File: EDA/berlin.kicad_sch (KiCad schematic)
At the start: 615 parts, among them J1 TYPE-C-31-M12_13, SW1,1 Rotary_Encoder_Switch_Chassis, SW1,10 MXSwitch, SW1,11 MXSwitch, SW1,12 MXSwitch, SW1,13 MXSwitch, SW1,14 MXSwitch, SW1,15 MXSwitch, SW1,16 Rotary_Encoder_Switch_Chassis, SW1,2 MXSwitch, SW1,3 MXSwitch, SW1,4 MXSwitch, SW1,5 MXSwitch, SW1,6 MXSwitch, SW1,7 MXSwitch, SW1,8 MXSwitch, SW1,9 MXSwitch, SW2,1 MXSwitch, SW2,10 MXSwitch, SW2,11 MXSwitch, SW2,12 MXSwitch, SW2,13 MXSwitch, SW2,14 MXSwitch, SW2,15 MXSwitch, SW2,16 MXSwitch, SW2,17 MXSwitch, SW2,18 MXSwitch, SW2,19 MXSwitch, SW2,2 MXSwitch, SW2,3 MXSwitch, SW2,4 MXSwitch, SW2,5 MXSwitch, SW2,6 MXSwitch, SW2,7 MXSwitch, SW2,9 MXSwitch, SW20-7,3 MXSwitch, SW3,1 MXSwitch, SW3,10 MXSwitch, SW3,11 MXSwitch, SW3,12 MXSwitch, SW3,13 MXSwitch, SW3,14 MXSwitch, SW3,15 MXSwitch, SW3,16 MXSwitch, SW3,17 MXSwitch, SW3,18 MXSwitch, SW3,19 MXSwitch, SW3,2 MXSwitch, SW3,3 MXSwitch, SW3,4 MXSwitch, SW3,5 MXSwitch, SW3,6 MXSwitch, SW3,7 MXSwitch, SW3,8 MXSwitch, SW3,9 MXSwitch, SW39-7,6 MXSwitch, SW4,1 MXSwitch, SW4,10 MXSwitch, SW4,11 MXSwitch, SW4,12 MXSwitch, SW4,13 MXSwitch, SW4,14 MXSwitch, SW4,15 MXSwitch, SW4,16 MXSwitch, SW4,17 MXSwitch, SW4,18 MXSwitch, SW4,19 MXSwitch, SW4,2 MXSwitch, SW4,3 MXSwitch, SW4,4 MXSwitch, SW4,5 MXSwitch, SW4,6 MXSwitch, SW4,7 MXSwitch, SW4,8 MXSwitch, SW4,9 MXSwitch, SW5,1 MXSwitch, SW5,10 MXSwitch, SW5,11 MXSwitch, SW5,12 MXSwitch, SW5,13 MXSwitch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

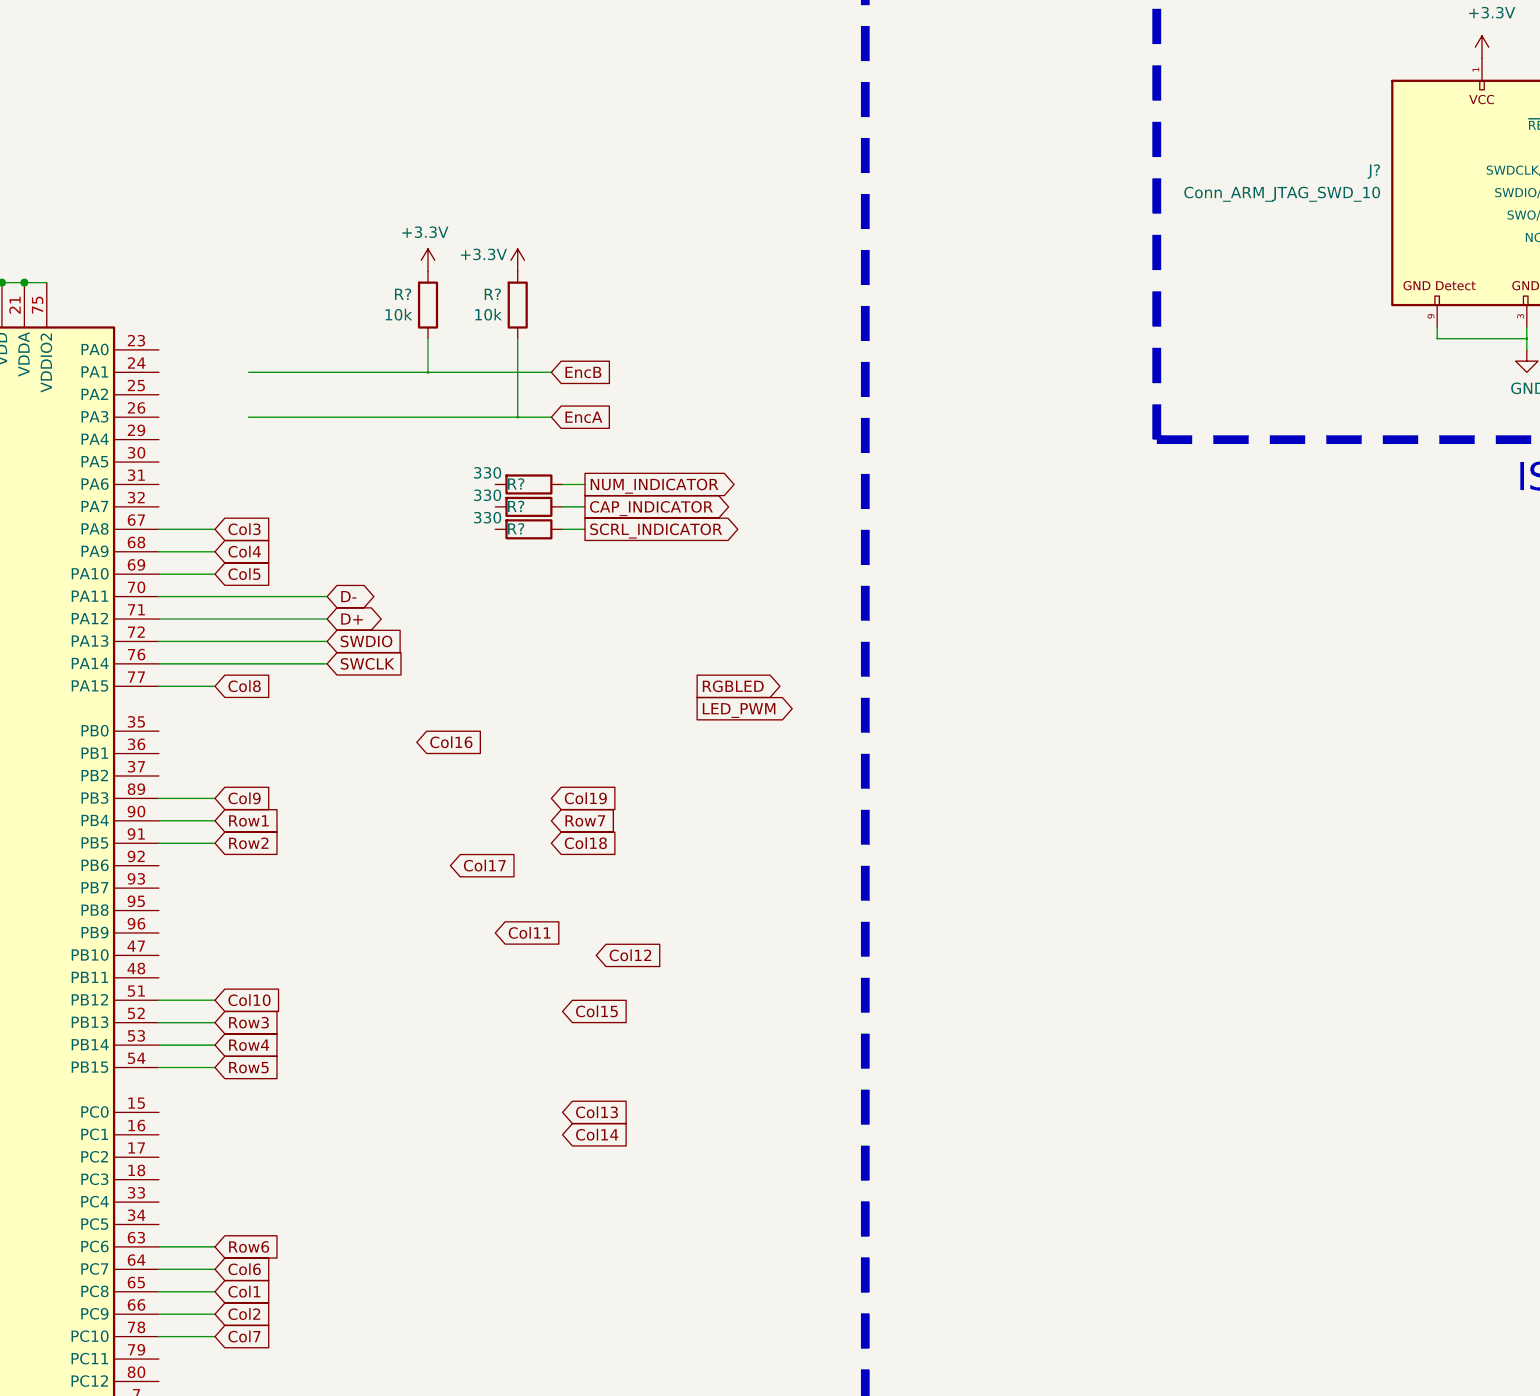
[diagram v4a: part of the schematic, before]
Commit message: route jtag and last key traces
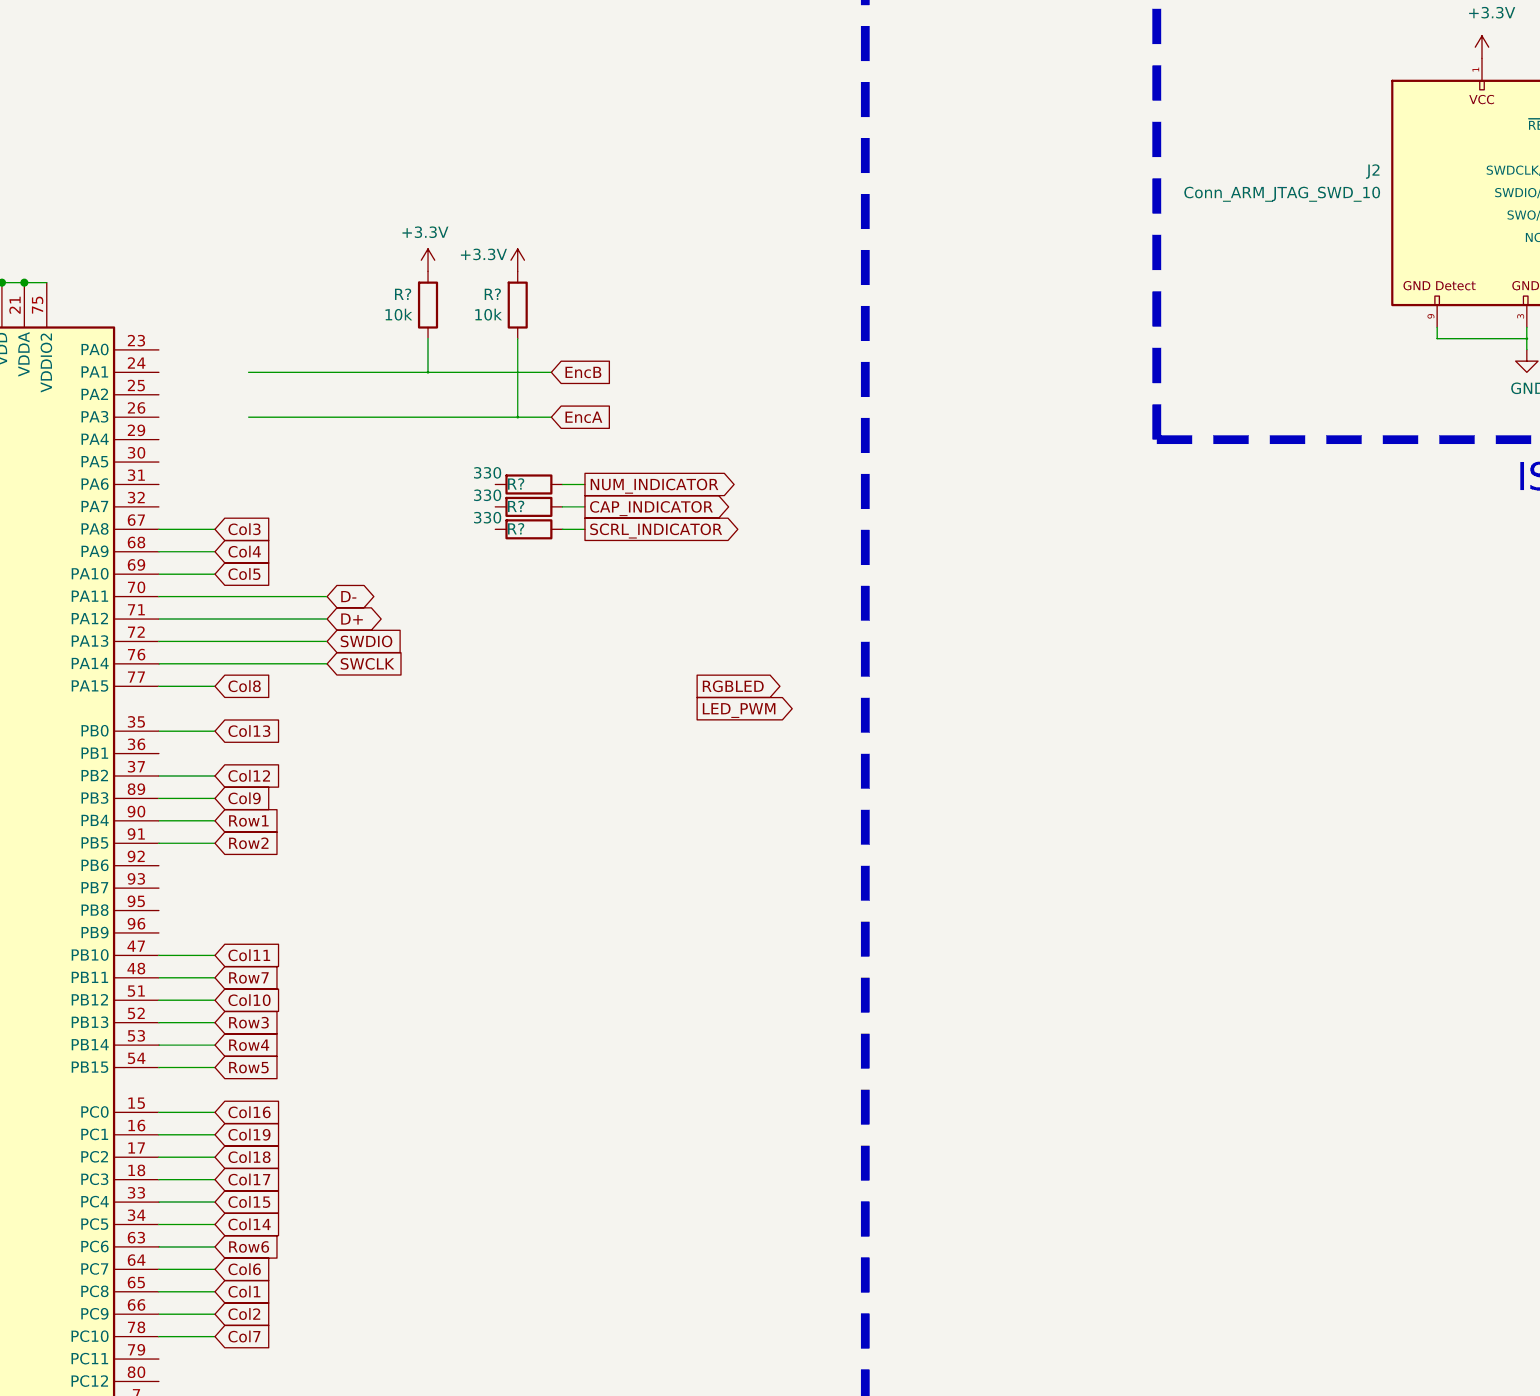
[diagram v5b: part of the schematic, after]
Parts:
- gave numbers to parts that had none: 1
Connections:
- net Col11: now also U1001.47 (PB10)
- net Col12: now also U1001.37 (PB2)
- net Col13: now also U1001.35 (PB0)
- net Col14: now also U1001.34 (PC5)
- net Col15: now also U1001.33 (PC4)
- net Col16: now also U1001.15 (PC0)
- net Col17: now also U1001.18 (PC3)
- net Col18: now also U1001.17 (PC2)
- net Col19: now also U1001.16 (PC1)
- net Row7: now also U1001.48 (PB11)
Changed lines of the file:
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@@
     (stroke (width 0) (type solid) (color 0 0 0 0))
   )
+  (wire (pts (xy 839.47 281.94) (xy 845.82 281.94))
+    (stroke (width 0) (type solid) (color 0 0 0 0))
+  )
+  (wire (pts (xy 839.47 287.02) (xy 845.82 287.02))
+    (stroke (width 0) (type solid) (color 0 0 0 0))
+  )
   (wire (pts (xy 839.47 289.56) (xy 845.82 289.56))
     (stroke (width 0) (type solid) (color 0 0 0 0))
@@
     (stroke (width 0) (type solid) (color 0 0 0 0))
   )
+  (wire (pts (xy 839.47 307.34) (xy 845.82 307.34))
+    (stroke (width 0) (type solid) (color 0 0 0 0))
+  )
+  (wire (pts (xy 839.47 309.88) (xy 845.82 309.88))
+    (stroke (width 0) (type solid) (color 0 0 0 0))
+  )
   (wire (pts (xy 839.47 312.42) (xy 845.82 312.42))
     (stroke (width 0) (type solid) (color 0 0 0 0))
@@
     (stroke (width 0) (type solid) (color 0 0 0 0))
   )
+  (wire (pts (xy 839.47 325.12) (xy 845.82 325.12))
+    (stroke (width 0) (type solid) (color 0 0 0 0))
+  )
+  (wire (pts (xy 839.47 327.66) (xy 845.82 327.66))
+    (stroke (width 0) (type solid) (color 0 0 0 0))
+  )
+  (wire (pts (xy 839.47 330.2) (xy 845.82 330.2))
+    (stroke (width 0) (type solid) (color 0 0 0 0))
+  )
+  (wire (pts (xy 839.47 332.74) (xy 845.82 332.74))
+    (stroke (width 0) (type solid) (color 0 0 0 0))
+  )
+  (wire (pts (xy 839.47 335.28) (xy 845.82 335.28))
+    (stroke (width 0) (type solid) (color 0 0 0 0))
+  )
+  (wire (pts (xy 839.47 337.82) (xy 845.82 337.82))
+    (stroke (width 0) (type solid) (color 0 0 0 0))
+  )
   (wire (pts (xy 839.47 340.36) (xy 845.82 340.36))
     (stroke (width 0) (type solid) (color 0 0 0 0))
@@
     )
   )
+  (global_label "Col13" (shape input) (at 845.82 281.94 0)
+    (effects (font (size 1.27 1.27)) (justify left))
+    (property "Intersheet References" "${INTERSHEET_REFS}" (id 0) (at 1294.13 -46.99 0)
+      (effects (font (size 1.27 1.27)) (justify left) hide)
+    )
+  )
+  (global_label "Col12" (shape input) (at 845.82 287.02 0)
+    (effects (font (size 1.27 1.27)) (justify left))
+    (property "Intersheet References" "${INTERSHEET_REFS}" (id 0) (at 1295.4 -34.29 0)
+      (effects (font (size 1.27 1.27)) (justify left) hide)
+    )
+  )
   (global_label "Col9" (shape input) (at 845.82 289.56 0)
     (effects (font (size 1.27 1.27)) (justify left))
@@
     )
   )
+  (global_label "Col11" (shape input) (at 845.82 307.34 0)
+    (effects (font (size 1.27 1.27)) (justify left))
+    (property "Intersheet References" "${INTERSHEET_REFS}" (id 0) (at 1295.4 -11.43 0)
+      (effects (font (size 1.27 1.27)) (justify left) hide)
+    )
+  )
+  (global_label "Row7" (shape input) (at 845.82 309.88 0)
+    (effects (font (size 1.27 1.27)) (justify left))
+    (property "Intersheet References" "${INTERSHEET_REFS}" (id 0) (at 353.06 -11.43 0)
+      (effects (font (size 1.27 1.27)) hide)
+    )
+  )
   (global_label "Col10" (shape input) (at 845.82 312.42 0)
     (effects (font (size 1.27 1.27)) (justify left))
@@
     )
   )
+  (global_label "Col16" (shape input) (at 845.82 325.12 0)
+    (effects (font (size 1.27 1.27)) (justify left))
+    (property "Intersheet References" "${INTERSHEET_REFS}" (id 0) (at 1294.13 21.59 0)
+      (effects (font (size 1.27 1.27)) (justify left) hide)
+    )
+  )
+  (global_label "Col19" (shape input) (at 845.82 327.66 0)
+    (effects (font (size 1.27 1.27)) (justify left))
+    (property "Intersheet References" "${INTERSHEET_REFS}" (id 0) (at 353.06 8.89 0)
+      (effects (font (size 1.27 1.27)) hide)
+    )
+  )
+  (global_label "Col18" (shape input) (at 845.82 330.2 0)
+    (effects (font (size 1.27 1.27)) (justify left))
+    (property "Intersheet References" "${INTERSHEET_REFS}" (id 0) (at 1294.13 36.83 0)
+      (effects (font (size 1.27 1.27)) (justify left) hide)
+    )
+  )
+  (global_label "Col17" (shape input) (at 845.82 332.74 0)
+    (effects (font (size 1.27 1.27)) (justify left))
+    (property "Intersheet References" "${INTERSHEET_REFS}" (id 0) (at 1294.13 26.67 0)
+      (effects (font (size 1.27 1.27)) (justify left) hide)
+    )
+  )
+  (global_label "Col15" (shape input) (at 845.82 335.28 0)
+    (effects (font (size 1.27 1.27)) (justify left))
+    (property "Intersheet References" "${INTERSHEET_REFS}" (id 0) (at 1295.4 1.27 0)
+      (effects (font (size 1.27 1.27)) (justify left) hide)
+    )
+  )
+  (global_label "Col14" (shape input) (at 845.82 337.82 0)
+    (effects (font (size 1.27 1.27)) (justify left))
+    (property "Intersheet References" "${INTERSHEET_REFS}" (id 0) (at 1295.4 6.35 0)
+      (effects (font (size 1.27 1.27)) (justify left) hide)
+    )
+  )
   (global_label "Row6" (shape input) (at 845.82 340.36 0)
     (effects (font (size 1.27 1.27)) (justify left))
@@
     )
   )
-  (global_label "Col16" (shape input) (at 868.68 283.21 0)
-    (effects (font (size 1.27 1.27)) (justify left))
-    (property "Intersheet References" "${INTERSHEET_REFS}" (id 0) (at 1316.99 -20.32 0)
-      (effects (font (size 1.27 1.27)) (justify left) hide)
-    )
-  )
-  (global_label "Col17" (shape input) (at 872.49 297.18 0)
-    (effects (font (size 1.27 1.27)) (justify left))
-    (property "Intersheet References" "${INTERSHEET_REFS}" (id 0) (at 1320.8 -8.89 0)
-      (effects (font (size 1.27 1.27)) (justify left) hide)
-    )
-  )
-  (global_label "Col11" (shape input) (at 877.57 304.8 0)
-    (effects (font (size 1.27 1.27)) (justify left))
-    (property "Intersheet References" "${INTERSHEET_REFS}" (id 0) (at 1327.15 -13.97 0)
-      (effects (font (size 1.27 1.27)) (justify left) hide)
-    )
-  )
   (global_label "EncB" (shape input) (at 883.92 241.3 0)
     (effects (font (size 1.27 1.27)) (justify left))
@@
     )
   )
-  (global_label "Col19" (shape input) (at 883.92 289.56 0)
-    (effects (font (size 1.27 1.27)) (justify left))
-    (property "Intersheet References" "${INTERSHEET_REFS}" (id 0) (at 391.16 -29.21 0)
-      (effects (font (size 1.27 1.27)) hide)
-    )
-  )
-  (global_label "Row7" (shape input) (at 883.92 292.1 0)
-    (effects (font (size 1.27 1.27)) (justify left))
-    (property "Intersheet References" "${INTERSHEET_REFS}" (id 0) (at 391.16 -29.21 0)
-      (effects (font (size 1.27 1.27)) hide)
-    )
-  )
-  (global_label "Col18" (shape input) (at 883.92 294.64 0)
-    (effects (font (size 1.27 1.27)) (justify left))
-    (property "Intersheet References" "${INTERSHEET_REFS}" (id 0) (at 1332.23 1.27 0)
-      (effects (font (size 1.27 1.27)) (justify left) hide)
-    )
-  )
-  (global_label "Col15" (shape input) (at 885.19 313.69 0)
-    (effects (font (size 1.27 1.27)) (justify left))
-    (property "Intersheet References" "${INTERSHEET_REFS}" (id 0) (at 1334.77 -20.32 0)
-      (effects (font (size 1.27 1.27)) (justify left) hide)
-    )
-  )
-  (global_label "Col13" (shape input) (at 885.19 325.12 0)
-    (effects (font (size 1.27 1.27)) (justify left))
-    (property "Intersheet References" "${INTERSHEET_REFS}" (id 0) (at 1333.5 -3.81 0)
-      (effects (font (size 1.27 1.27)) (justify left) hide)
-    )
-  )
-  (global_label "Col14" (shape input) (at 885.19 327.66 0)
-    (effects (font (size 1.27 1.27)) (justify left))
-    (property "Intersheet References" "${INTERSHEET_REFS}" (id 0) (at 1334.77 -3.81 0)
-      (effects (font (size 1.27 1.27)) (justify left) hide)
-    )
-  )
   (global_label "NUM_INDICATOR" (shape output) (at 887.73 254 0)
     (effects (font (size 1.27 1.27)) (justify left))
@@
     )
   )
-  (global_label "Col12" (shape input) (at 889 307.34 0)
-    (effects (font (size 1.27 1.27)) (justify left))
-    (property "Intersheet References" "${INTERSHEET_REFS}" (id 0) (at 1338.58 -13.97 0)
-      (effects (font (size 1.27 1.27)) (justify left) hide)
-    )
-  )
   (global_label "RGBLED" (shape output) (at 900.43 276.86 0)
     (effects (font (size 1.27 1.27)) (justify left))
@@
   (symbol (lib_id "acheronSymbols:Conn_ARM_JTAG_SWD_10") (at 989.33 220.98 0) (unit 1)
     (in_bom yes) (on_board yes)
-    (property "Reference" "J?" (id 0) (at 977.9 218.44 0)
+    (property "Reference" "J2" (id 0) (at 977.9 218.44 0)
       (effects (font (size 1.27 1.27)) (justify right))
     )
@@
     )
     (path "/710526a9-81ec-4341-af20-73d8794d58c7"
-      (reference "J?") (unit 1) (value "Conn_ARM_JTAG_SWD_10") (footprint "Connector_PinSocket_2.54mm:PinSocket_2x05_P2.54mm_Vertical")
+      (reference "J2") (unit 1) (value "Conn_ARM_JTAG_SWD_10") (footprint "Connector_PinSocket_2.54mm:PinSocket_2x05_P2.54mm_Vertical")
     )
     (path "/455c4cbb-3d0b-48d2-aa90-82ba22ea7714"

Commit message: small updates in naming/routing
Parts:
- gave numbers to parts that had none: 11
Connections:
- net GND: now also R706.2; no longer R706.1
- net at J1.B5 (CC2): now also R706.1; no longer R706.2
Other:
- moved on the sheet: R706
